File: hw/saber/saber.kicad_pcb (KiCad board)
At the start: 2 copper layers, 115.6 x 82.5 mm, 80 parts, among them J1 Screw_Terminal_01x02, J2 Screw_Terminal_01x02, J3 Screw_Terminal_01x12, J4 NUCLEO144ZE-STLINK, Q1 STL76DN4LF7AG, Q2 STL120N4F6AG, Q3 SSM3K337R, Q4 SIS413DN-T1-GE3, Q5 SSM3K337R, Q6 SSM3K337R, Q7 SSM3K337R, SW1 SW, U1 STM32L031F4Px, U2 VNHD7008AY, U3 AZ1117IH-3.3TRG1, U4 MMA8452Q

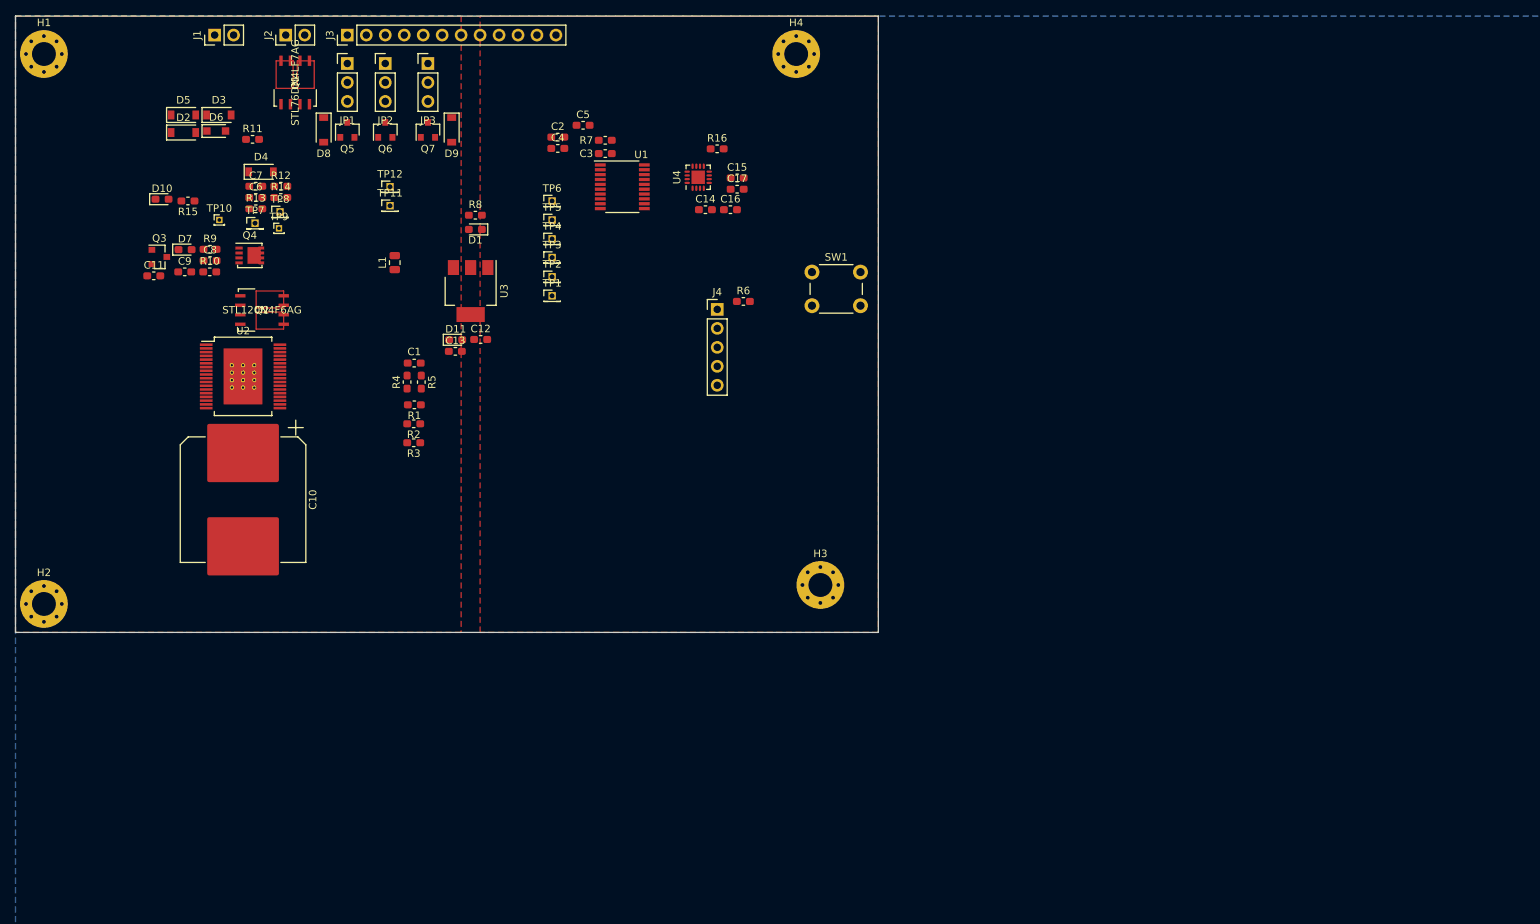
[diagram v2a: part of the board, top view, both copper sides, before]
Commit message: rechose diodes for density
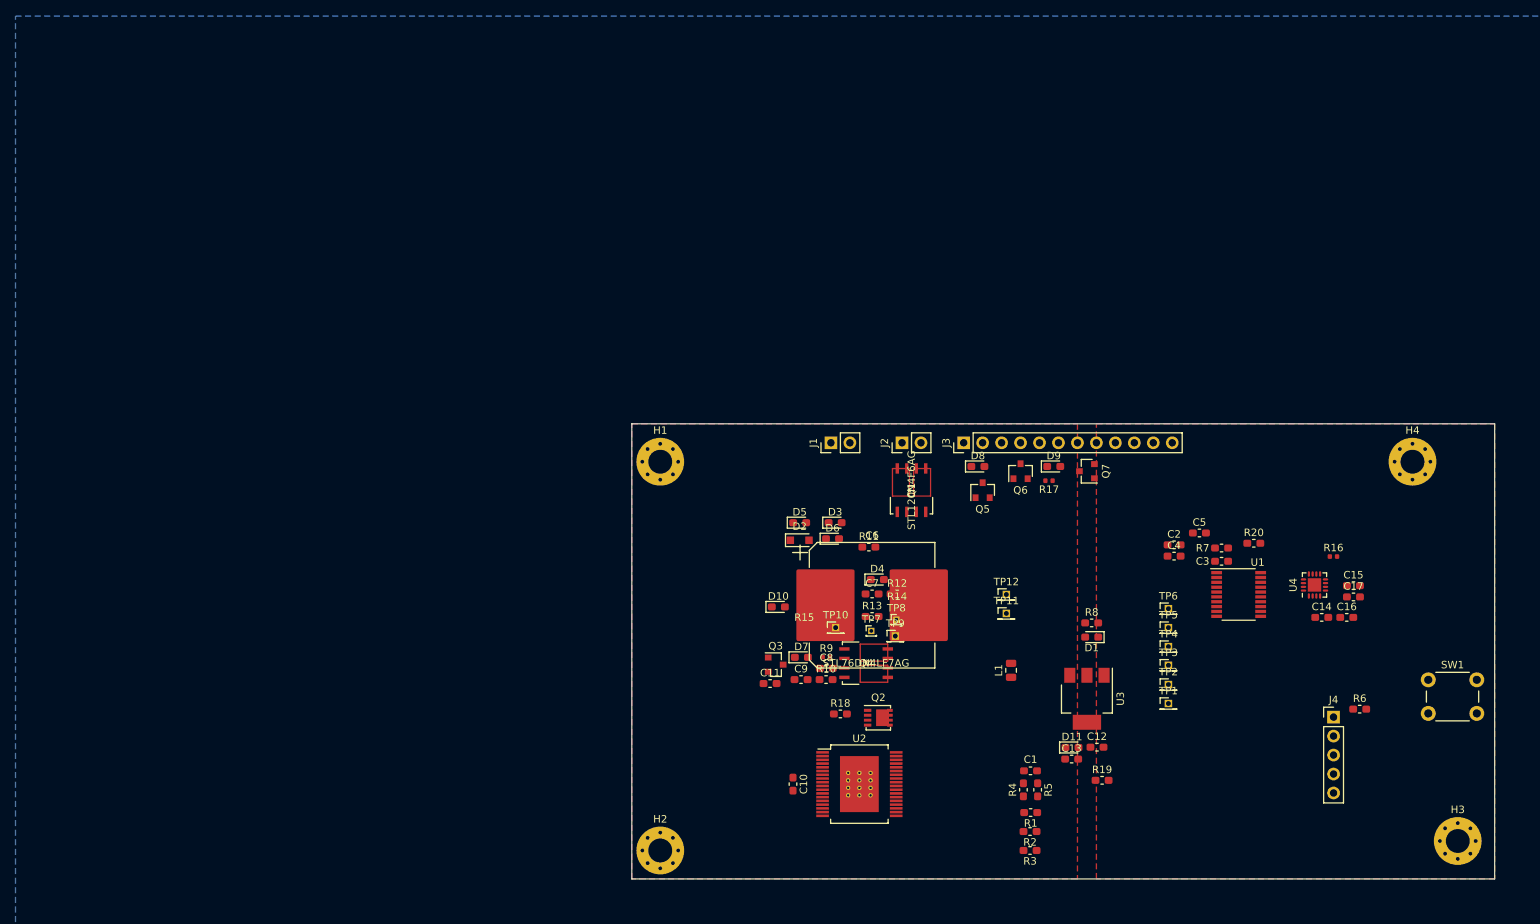
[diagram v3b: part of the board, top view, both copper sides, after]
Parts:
- removed JP1, JP2, JP3: Jumper_3_Bridged12, Connector_PinHeader_2.54mm:PinHeader_1x03_P2.54mm_Vertical
- added R17: 0, Resistor_SMD:R_0402_1005Metric, F.Cu at (151.1, 74.9)
- added R18: 10k, Resistor_SMD:R_0603_1608Metric_Pad1.05x0.95mm_HandSolder, F.Cu at (123.2, 106.2)
- added R19: 1k, Resistor_SMD:R_0603_1608Metric_Pad1.05x0.95mm_HandSolder, F.Cu at (158.2, 115.1)
- added R20: 1k, Resistor_SMD:R_0603_1608Metric_Pad1.05x0.95mm_HandSolder, F.Cu at (178.6, 83.3)
- C10: value 470u -> 10n; footprint Capacitor_SMD:CP_Elec_16x17.5 -> Capacitor_SMD:C_0603_1608Metric_Pad1.05x0.95mm_HandSolder
- C11, C9: value 100n -> 10n
- C16: value 100n -> 4u7
- C17: value 4u7 -> 100n
- C6: value 10n -> 470u; footprint Capacitor_SMD:C_0603_1608Metric_Pad1.05x0.95mm_HandSolder -> Capacitor_SMD:CP_Elec_16x17.5
- C7, C8: value 10n -> 100n
- D2: value CDSW4448-G -> BZT52C8V2S-7-F; footprint Diode_SMD:D_SOD-123 -> Diode_SMD:D_SOD-323_HandSoldering
- D3: value CDSW4448-G -> 150060RS75020; footprint Diode_SMD:D_SOD-123 -> LED_SMD:LED_0603_1608Metric_Pad1.05x0.95mm_HandSolder
- D4, D5, D8, D9: value CDSW4448-G -> SDM2U30CSP-7; footprint Diode_SMD:D_SOD-123 -> Diode_SMD:D_0603_1608Metric_Pad1.05x0.95mm_HandSolder
- D6: value BZT52C8V2S-7-F -> SDM2U30CSP-7; footprint Diode_SMD:D_SOD-323_HandSoldering -> Diode_SMD:D_0603_1608Metric_Pad1.05x0.95mm_HandSolder
- D7: value 150060RS75020 -> SDM2U30CSP-7; footprint LED_SMD:LED_0603_1608Metric_Pad1.05x0.95mm_HandSolder -> Diode_SMD:D_0603_1608Metric_Pad1.05x0.95mm_HandSolder
- Q1: value STL76DN4LF7AG -> STL120N4F6AG; footprint STL76DN4LF7AG:STL76DN4LF7AG -> STL120N4F6AG:STL120N4F6AG
- Q2: value STL120N4F6AG -> SIS413DN-T1-GE3; footprint STL120N4F6AG:STL120N4F6AG -> Package_SO:Vishay_PowerPAK_1212-8_Single
- Q4: value SIS413DN-T1-GE3 -> STL76DN4LF7AG; footprint Package_SO:Vishay_PowerPAK_1212-8_Single -> STL76DN4LF7AG:STL76DN4LF7AG
- R10: value 0 -> 1k
- R11: value 1k -> 1K
- R12: value 1k -> 10k
- R13: value 1K -> 10k
- R14, R9: value 10k -> 0; footprint Resistor_SMD:R_0603_1608Metric_Pad1.05x0.95mm_HandSolder -> Resistor_SMD:R_0402_1005Metric
- R15, R16: value 1k -> 0; footprint Resistor_SMD:R_0603_1608Metric_Pad1.05x0.95mm_HandSolder -> Resistor_SMD:R_0402_1005Metric
- R4: value 1k5 -> 10k
- R5: value 10k -> 1k5
- R8: value 10k -> 1k
- TP10, TP9: footprint Connector_PinHeader_1.00mm:PinHeader_1x01_P1.00mm_Vertical -> Connector_PinHeader_1.27mm:PinHeader_1x01_P1.27mm_Vertical
- TP7, TP8: footprint Connector_PinHeader_1.27mm:PinHeader_1x01_P1.27mm_Vertical -> Connector_PinHeader_1.00mm:PinHeader_1x01_P1.00mm_Vertical
- moved Q7 99.4 mm to (156.2, 73.7), turned to 180 degrees
- moved D11 99.0 mm to (154.2, 110.7)
- moved Q2 99.0 mm to (128.3, 106.7)
- moved TP9 99.0 mm to (130.5, 95.7)
- moved C11 99.0 mm to (113.8, 102.1)
- moved C14 99.0 mm to (187.7, 93.2)
- moved C15 99.0 mm to (191.9, 89.0)
- moved C17 99.0 mm to (191.9, 90.5)
- moved C3 99.0 mm to (174.2, 85.7)
- moved C5 99.0 mm to (171.3, 81.9)
- moved C6 99.0 mm to (127.4, 91.6)
- moved C7 99.0 mm to (127.4, 90.1)
- moved C8 99.0 mm to (121.3, 100.1)
- moved C9 99.0 mm to (117.9, 101.6)
- moved D1 99.0 mm to (156.8, 95.9)
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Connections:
- C10 pad 1: Net-(C10-Pad1) -> /MOT+
- C11 pad 1: Net-(C10-Pad1) -> /MOT-
- C14 pad 2: Net-(C14-Pad2) -> +3V3
- C17 pad 2: +3V3 -> Net-(C17-Pad2)
- C6 pad 1: /MOT+ -> Net-(C6-Pad1)
- C7 pad 1: /MOT- -> Net-(C6-Pad1)
- C7 pad 2: /MOT+ -> GND
- C8 pad 1: /MOT- -> Net-(C8-Pad1)
- C9 pad 1: Net-(C9-Pad1) -> /MOT-
- C9 pad 2: GND -> /MOT+
- D2 pad 1: /BATT+ -> Net-(C6-Pad1)
- D2 pad 2: /MOT+ -> Net-(D2-Pad2)
- D3 pad 1: /MOT+ -> GND
- D3 pad 2: GND -> Net-(D3-Pad2)
- D4 pad 2: /MOT- -> /MOT+
- D5 pad 1: /MOT- -> /BATT+
- D5 pad 2: GND -> /MOT-
- D6 pad 1: Net-(C10-Pad1) -> /MOT+
- D6 pad 2: Net-(D6-Pad2) -> GND
- D7 pad 1: GND -> /MOT-
- D7 pad 2: Net-(D7-Pad2) -> GND
- D8 pad 1: /SOL+ -> +12V
- J3 pad 1: /SOL+ -> +12V
- Q1 pad 1: GND -> Net-(C6-Pad1)
- Q1 pad 2: Net-(Q1-Pad2) -> Net-(C6-Pad1)
- Q1 pad 3: GND -> Net-(C6-Pad1)
- Q1 pad 5: /MOT+ -> /BATT+
- Q1 pad 6: /MOT+ -> /BATT+
- Q1 pad 7: /MOT- -> /BATT+
- Q1 pad 8: /MOT- -> /BATT+
- Q2 pad 1: Net-(C10-Pad1) -> Net-(Q2-Pad1)
- Q2 pad 2: Net-(C10-Pad1) -> +12V
- Q2 pad 3: Net-(C10-Pad1) -> Net-(C6-Pad1)
- Q2 pad 4: Net-(Q2-Pad4) -> (no net)
- Q2 pad 5: /BATT+ -> (no net)
- Q3 pad 3: Net-(Q3-Pad3) -> Net-(Q2-Pad1)
- Q4 pad 1: Net-(Q3-Pad3) -> GND
- Q4 pad 2: +12V -> Net-(Q4-Pad2)
- Q4 pad 3: Net-(C10-Pad1) -> GND
- Q4 pad 4: (no net) -> Net-(Q4-Pad4)
- Q4 pad 5: (no net) -> /MOT+
- R10 pad 1: Net-(Q3-Pad1) -> GND
- R10 pad 2: Net-(D6-Pad2) -> Net-(Q3-Pad1)
- R11 pad 1: GND -> Net-(Q2-Pad1)
- R11 pad 2: Net-(Q3-Pad1) -> Net-(D3-Pad2)
- R12 pad 1: Net-(C10-Pad1) -> Net-(R12-Pad1)
- R12 pad 2: Net-(Q3-Pad3) -> GND
- R13 pad 1: Net-(Q3-Pad3) -> Net-(R13-Pad1)
- R13 pad 2: Net-(D7-Pad2) -> GND
- R14 pad 1: +12V -> /LED+
- R14 pad 2: Net-(D10-Pad2) -> +12V
- R15 pad 2: Net-(D11-Pad2) -> /LED+
- R16 pad 1: Net-(R16-Pad1) -> /SPKR+
- R16 pad 2: GND -> +12V
- R4 pad 1: /hbridge/imtr -> /micro/ADC_imtr
- R4 pad 2: GND -> /hbridge/imtr
- R5 pad 1: /micro/ADC_imtr -> /hbridge/imtr
- R5 pad 2: /hbridge/imtr -> GND
- R6 pad 1: /micro/BOOT0 -> Net-(D1-Pad2)
- R6 pad 2: GND -> /micro/LED_HBEAT
- R7 pad 1: Net-(D1-Pad2) -> /micro/BOOT0
- R7 pad 2: /micro/LED_HBEAT -> GND
- R8 pad 1: Net-(R8-Pad1) -> Net-(C6-Pad1)
- R8 pad 2: GND -> Net-(Q2-Pad1)
- R9 pad 1: Net-(R9-Pad1) -> Net-(Q3-Pad1)
- R9 pad 2: GND -> Net-(D2-Pad2)
- TP10 pad 1: Net-(Q3-Pad3) -> Net-(Q4-Pad4)
- TP2 pad 1: /micro/INA_MCU -> /acc/SDA
- TP3 pad 1: /micro/INB_MCU -> /micro/INA_MCU
- TP4 pad 1: /actuators/PWM_SPKR -> /micro/INB_MCU
- TP5 pad 1: /acc/SDA -> /acc/SCL
- TP6 pad 1: /acc/SCL -> /actuators/PWM_SPKR
- TP7 pad 1: Net-(Q1-Pad4) -> Net-(Q2-Pad1)
- TP8 pad 1: Net-(Q1-Pad2) -> Net-(Q3-Pad1)
- TP9 pad 1: Net-(Q3-Pad1) -> Net-(Q4-Pad2)
- U2 pad 13: Net-(Q1-Pad4) -> Net-(Q4-Pad4)
- U2 pad 15: Net-(R8-Pad1) -> Net-(R12-Pad1)
- U2 pad 17: Net-(Q2-Pad4) -> Net-(Q1-Pad4)
- U2 pad 22: Net-(R9-Pad1) -> Net-(R13-Pad1)
- U2 pad 24: Net-(Q1-Pad2) -> Net-(Q4-Pad2)
- U2 pad 25: Net-(C9-Pad1) -> Net-(C8-Pad1)
- U2 pad 37: Net-(C10-Pad1) -> Net-(C6-Pad1)
- U4 pad 10: GND -> (no net)
- U4 pad 2: Net-(C14-Pad2) -> Net-(C17-Pad2)
- U4 pad 7: Net-(R16-Pad1) -> Net-(R20-Pad1)
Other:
- board size 115.6 x 82.5 mm -> 115.6 x 61 mm

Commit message: pre-datasheet-review placement
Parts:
- removed TP11, TP12: TestPoint, Connector_PinHeader_1.27mm:PinHeader_1x01_P1.27mm_Vertical
- removed TP7, TP8: TestPoint, Connector_PinHeader_1.00mm:PinHeader_1x01_P1.00mm_Vertical
- C9, D8, D9: moved to B.Cu
- J1, J2: footprint Connector_PinHeader_2.54mm:PinHeader_1x02_P2.54mm_Vertical -> TerminalBlock_Phoenix:TerminalBlock_Phoenix_MPT-0,5-2-2.54_1x02_P2.54mm_Horizontal
- J3: footprint Connector_PinHeader_2.54mm:PinHeader_1x12_P2.54mm_Vertical -> TerminalBlock_Phoenix:TerminalBlock_Phoenix_MPT-0,5-12-2.54_1x12_P2.54mm_Horizontal
- Q1: value STL120N4F6AG -> (none)
- Q4: value STL76DN4LF7AG -> (none)
- R9: footprint Resistor_SMD:R_0402_1005Metric -> Resistor_SMD:R_0603_1608Metric_Pad1.05x0.95mm_HandSolder
- TP1, TP10, TP2, TP3, TP4, TP5, TP6, TP9: footprint Connector_PinHeader_1.27mm:PinHeader_1x01_P1.27mm_Vertical -> Connector_PinHeader_1.00mm:PinHeader_1x01_P1.00mm_Vertical
- moved 12V 71.4 mm to (185.5, 102.4), turned to 180 degrees
- moved VbL 66.1 mm to (185.5, 100.7), turned to 180 degrees
- moved R18 58.9 mm to (181.9, 102.4)
- moved R11 57.5 mm to (181.9, 100.7)
- moved C10 48.8 mm to (136.9, 71.1), turned to 90 degrees
- moved Q3 38.4 mm to (151.4, 88.9)
- moved SW1 36.5 mm to (175.8, 76.2), turned to 90 degrees
- moved R15 35.1 mm to (149.9, 76.7), turned to 90 degrees
- moved C11 34.3 mm to (128.5, 71.1), turned to 90 degrees
- moved R16 33.6 mm to (156.7, 76.7), turned to 270 degrees
- moved 3V3 32.0 mm to (185.5, 104.1), turned to 180 degrees
- moved C9 31.3 mm to (132.7, 74.0), turned to 180 degrees
- moved R10 30.4 mm to (148.8, 88.8), turned to 270 degrees
- moved R3 29.9 mm to (147.8, 94.6)
- moved Q2 29.8 mm to (148.8, 85.1), turned to 180 degrees
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- renumbered D10 to 12V, D11 to 3V3, H1 to ?, H2 to ?, H3 to ?, H4 to ?, D1 to HB, D3 to VbL
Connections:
- net Net-(C6-Pad1) renamed /hbridge/VCC
- Q4 pad 5: /MOT+ -> /MOT-
- Q4 pad 6: /MOT+ -> /MOT-
- Q4 pad 7: /MOT- -> /MOT+
- Q4 pad 8: /MOT- -> /MOT+
- TP10 pad 1: Net-(Q4-Pad4) -> Net-(Q4-Pad2)
- TP9 pad 1: Net-(Q4-Pad2) -> Net-(Q4-Pad4)
- U2 pad 13: Net-(Q4-Pad4) -> Net-(Q4-Pad2)
- U2 pad 24: Net-(Q4-Pad2) -> Net-(Q4-Pad4)
- U4 pad 10: (no net) -> GND
- U4 pad 11: Net-(U4-Pad11) -> /acc/SCL
- U4 pad 2: Net-(C17-Pad2) -> Net-(R20-Pad1)
- U4 pad 4: /acc/SCL -> Net-(U4-Pad4)
- U4 pad 6: /acc/SDA -> Net-(U4-Pad6)
- U4 pad 7: Net-(R20-Pad1) -> Net-(C17-Pad2)
- U4 pad 9: Net-(U4-Pad9) -> /acc/SDA
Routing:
- net /hbridge/PWM_MTR: track 0.00 -> 0.71 mm
- net /hbridge/imtr: track 0.00 -> 0.68 mm
- added copper zone on F.Cu, net /BATT+
- added copper zone on F.Cu, net /hbridge/VCC
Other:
- board size 115.6 x 61 mm -> 87.6 x 47 mm

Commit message: 4 layer board for density. Need to re-choose motor cap
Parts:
- removed 12V, 3V3: 150060AS75000, LED_SMD:LED_0603_1608Metric_Pad1.05x0.95mm_HandSolder
- removed ? (x4): MountingHole_Pad, MountingHole:MountingHole_3.2mm_M3_Pad_Via
- removed C6: 470u, Capacitor_SMD:CP_Elec_16x17.5
- removed HB: 150060VS75020, LED_SMD:LED_0603_1608Metric_Pad1.05x0.95mm_HandSolder
- removed VbL: 150060RS75020, LED_SMD:LED_0603_1608Metric_Pad1.05x0.95mm_HandSolder
- added D1: 150060VS75020, LED_SMD:LED_0603_1608Metric_Pad1.05x0.95mm_HandSolder, F.Cu at (157.6, 91.3)
- added D10: 150060AS75000, LED_SMD:LED_0603_1608Metric_Pad1.05x0.95mm_HandSolder, F.Cu at (152.4, 91.3)
- added D11: 150060AS75000, LED_SMD:LED_0603_1608Metric_Pad1.05x0.95mm_HandSolder, F.Cu at (154.2, 91.3)
- added D3: 150060RS75020, LED_SMD:LED_0603_1608Metric_Pad1.05x0.95mm_HandSolder, F.Cu at (155.9, 91.3)
- added H1: MountingHole_Pad, MountingHole:MountingHole_3.2mm_M3_Pad_Via, F.Cu at (108.0, 72.4)
- added H2: MountingHole_Pad, MountingHole:MountingHole_3.2mm_M3_Pad_Via, F.Cu at (108.0, 90.8)
- added H3: MountingHole_Pad, MountingHole:MountingHole_3.2mm_M3_Pad_Via, F.Cu at (179.1, 72.4)
- added H4: MountingHole_Pad, MountingHole:MountingHole_3.2mm_M3_Pad_Via, F.Cu at (179.1, 90.8)
- added REF**: CP_Elec_8x10, Capacitor_SMD:CP_Elec_8x10, F.Cu at (116.8, 89.4)
- C12, C13, C14, C15, C16, C17, C2, C3, C4, C5, D2, L1, Q2, Q3, R10, R20, R7, R8, R9, U1, U3, U4: moved to B.Cu
- Q1: value (none) -> STL120N4F6AG
- Q4: value (none) -> STL76DN4LF7AG
- moved R19 33.9 mm to (152.4, 87.5), turned to 270 degrees
- moved C12 32.9 mm to (131.8, 80.4), turned to 0 degrees
- moved L1 32.2 mm to (131.8, 82.3), turned to 180 degrees
- moved C13 32.1 mm to (141.4, 84.4), turned to 270 degrees
- moved TP1 31.7 mm to (143.0, 92.7), turned to 270 degrees
- moved R18 31.5 mm to (154.2, 87.5), turned to 270 degrees
- moved R11 29.3 mm to (155.9, 87.5), turned to 270 degrees
- moved U3 28.6 mm to (137.3, 87.1)
- moved TP3 27.6 mm to (145.5, 92.7), turned to 270 degrees
- moved J4 27.6 mm to (162.6, 92.7), turned to 90 degrees
- moved R6 26.9 mm to (157.6, 87.5), turned to 90 degrees
- moved Q3 24.6 mm to (127.0, 85.4), turned to 270 degrees
- moved R8 24.1 mm to (128.9, 89.2), turned to 90 degrees
- moved TP4 24.0 mm to (148.1, 92.7), turned to 270 degrees
- moved R9 23.8 mm to (123.5, 86.4), turned to 180 degrees
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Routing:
- added copper zone on In2.Cu, net +12V
- added copper zone on In2.Cu, net +3V3
- added copper zone on In2.Cu, net /BATT+
- added copper zone on In2.Cu, net /hbridge/VCC
- added copper zone on In1.Cu, net GND
- removed copper zone on F.Cu, net +12V
- removed copper zone on F.Cu, net +3V3
- removed copper zone on F.Cu, net /BATT+
- removed copper zone on F.Cu, net /hbridge/VCC
- removed copper zone on B.Cu, net GND
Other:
- board size 87.6 x 47 mm -> 81.3 x 28.6 mm
- copper layers 2 -> 4

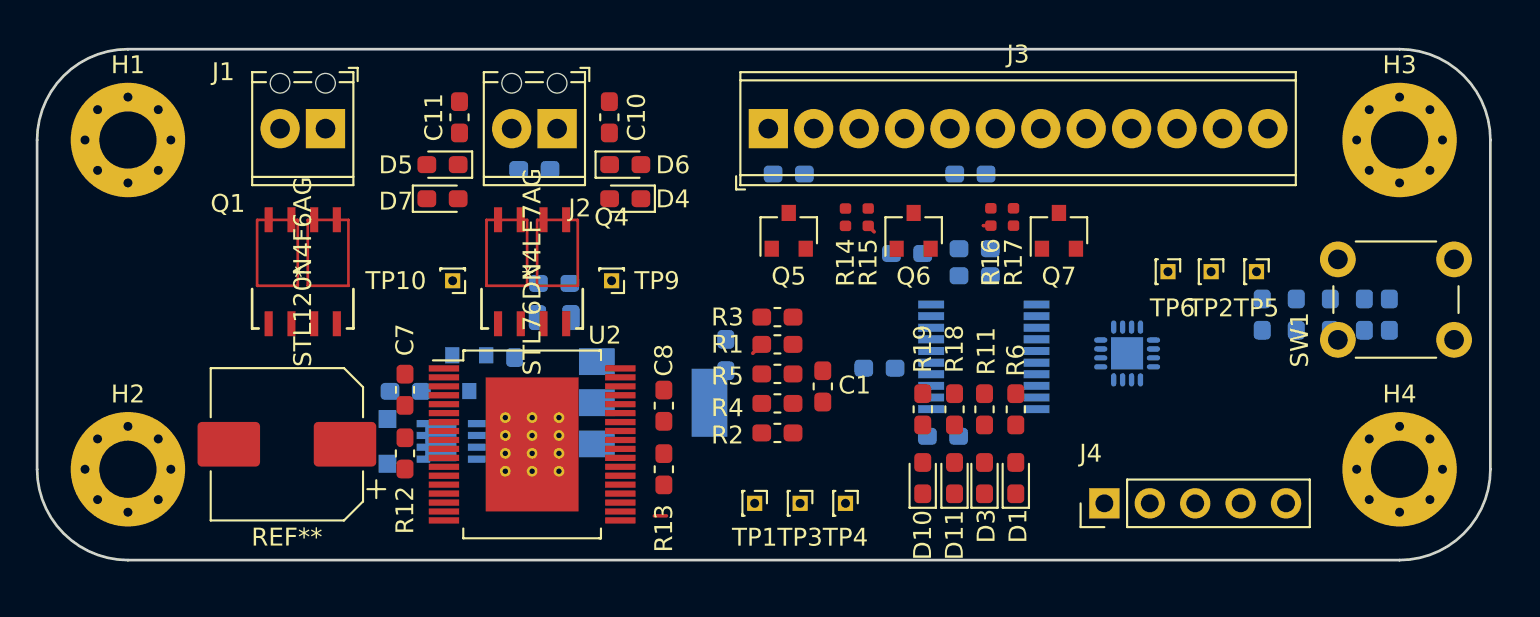
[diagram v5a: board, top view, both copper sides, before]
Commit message: additional layout changes for density
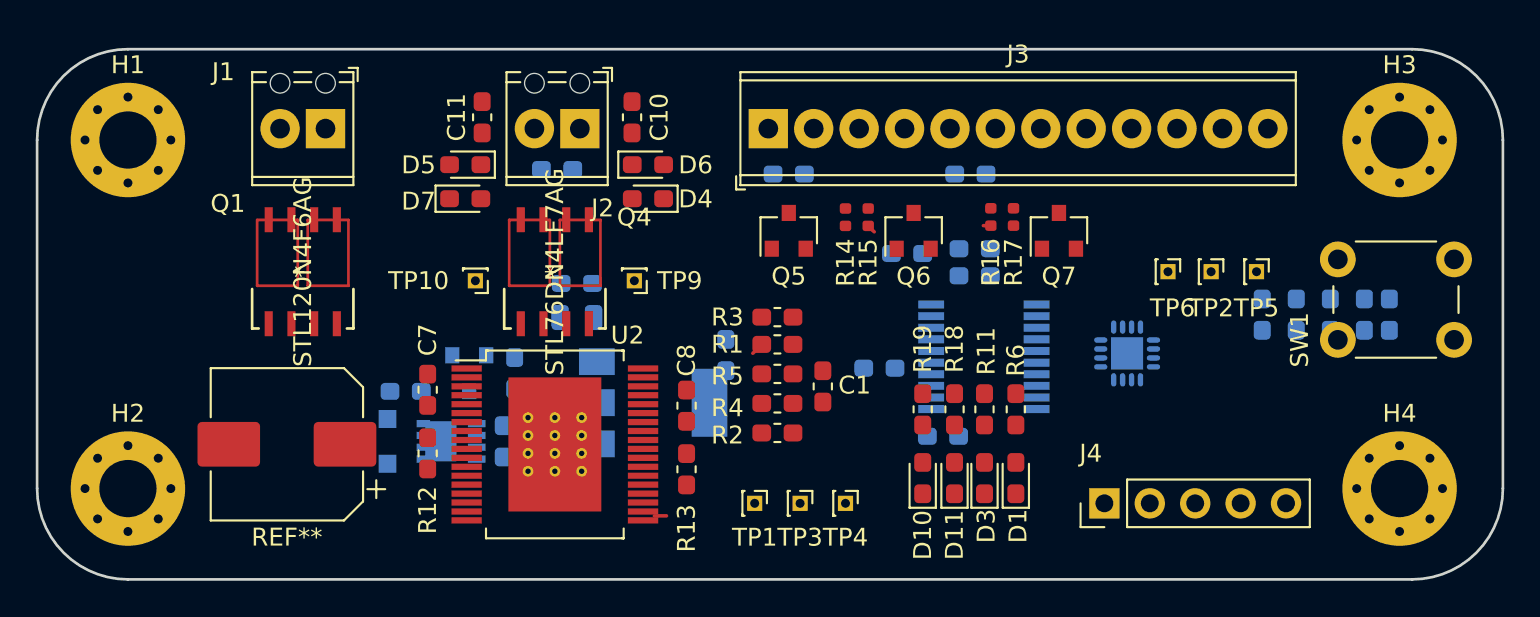
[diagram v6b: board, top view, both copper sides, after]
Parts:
- moved C10 1.27 mm to (136.1, 71.1)
- moved C8 1.27 mm to (139.2, 87.2)
- moved C9 1.27 mm to (132.0, 74.0)
- moved J2 1.27 mm to (133.2, 71.8)
- moved R13 1.27 mm to (139.2, 90.8)
- moved C11 1.27 mm to (127.8, 71.1)
- moved C7 1.27 mm to (124.7, 86.4)
- moved D5 1.27 mm to (126.8, 75.7)
- moved D7 1.27 mm to (126.8, 73.8)
- moved R12 1.27 mm to (124.7, 89.9)
- moved TP10 1.27 mm to (127.4, 80.3)
- moved C12 1.27 mm to (133.1, 80.4)
- moved D4 1.27 mm to (137.0, 75.7)
- moved D6 1.27 mm to (137.0, 73.8)
- moved L1 1.27 mm to (133.1, 82.3)
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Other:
- board size 81.3 x 28.6 mm -> 82 x 29.7 mm
